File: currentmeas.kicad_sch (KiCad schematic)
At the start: 14 parts, among them U3 CSE7759B

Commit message: Renamed things. Removed reference image. Ready for the world.
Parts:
- U3: symbol merossspecific:CSE7759B -> designspecific:CSE7759B
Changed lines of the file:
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@@
 		)
 		(instances
-			(project "Meross smart outlet reverse"
+			(project "smart-outlet-m-reverse"
 				(path "/0b789f5a-74d1-4f81-bd1f-7ac838c6392e/64da09b2-a22e-4689-a149-b317ef83cf14"
 					(reference "R14")
@@
 		)
 		(instances
-			(project "Meross smart outlet reverse"
+			(project "smart-outlet-m-reverse"
 				(path "/0b789f5a-74d1-4f81-bd1f-7ac838c6392e/64da09b2-a22e-4689-a149-b317ef83cf14"
 					(reference "#PWR06")
@@
 		)
 		(instances
-			(project "Meross smart outlet reverse"
+			(project "smart-outlet-m-reverse"
 				(path "/0b789f5a-74d1-4f81-bd1f-7ac838c6392e/64da09b2-a22e-4689-a149-b317ef83cf14"
 					(reference "R13")
@@
 		)
 		(instances
-			(project "Meross smart outlet reverse"
+			(project "smart-outlet-m-reverse"
 				(path "/0b789f5a-74d1-4f81-bd1f-7ac838c6392e/64da09b2-a22e-4689-a149-b317ef83cf14"
 					(reference "C16")
@@
 		)
 		(instances
-			(project "Meross smart outlet reverse"
+			(project "smart-outlet-m-reverse"
 				(path "/0b789f5a-74d1-4f81-bd1f-7ac838c6392e/64da09b2-a22e-4689-a149-b317ef83cf14"
 					(reference "R15")
@@
 		)
 		(instances
-			(project "Meross smart outlet reverse"
+			(project "smart-outlet-m-reverse"
 				(path "/0b789f5a-74d1-4f81-bd1f-7ac838c6392e/64da09b2-a22e-4689-a149-b317ef83cf14"
 					(reference "R20")
@@
 		)
 		(instances
-			(project "Meross smart outlet reverse"
+			(project "smart-outlet-m-reverse"
 				(path "/0b789f5a-74d1-4f81-bd1f-7ac838c6392e/64da09b2-a22e-4689-a149-b317ef83cf14"
 					(reference "#PWR05")
@@
 		)
 		(instances
-			(project "Meross smart outlet reverse"
+			(project "smart-outlet-m-reverse"
 				(path "/0b789f5a-74d1-4f81-bd1f-7ac838c6392e/64da09b2-a22e-4689-a149-b317ef83cf14"
 					(reference "R16")
@@
 		)
 		(instances
-			(project "Meross smart outlet reverse"
+			(project "smart-outlet-m-reverse"
 				(path "/0b789f5a-74d1-4f81-bd1f-7ac838c6392e/64da09b2-a22e-4689-a149-b317ef83cf14"
 					(reference "#PWR04")
@@
 		)
 		(instances
-			(project "Meross smart outlet reverse"
+			(project "smart-outlet-m-reverse"
 				(path "/0b789f5a-74d1-4f81-bd1f-7ac838c6392e/64da09b2-a22e-4689-a149-b317ef83cf14"
 					(reference "#PWR019")
@@
 		)
 		(instances
-			(project "Meross smart outlet reverse"
+			(project "smart-outlet-m-reverse"
 				(path "/0b789f5a-74d1-4f81-bd1f-7ac838c6392e/64da09b2-a22e-4689-a149-b317ef83cf14"
 					(reference "C19")
@@
 	)
 	(symbol
-		(lib_id "merossspecific:CSE7759B")
+		(lib_id "designspecific:CSE7759B")
 		(at 170.18 85.09 0)
 		(unit 1)
@@
 		)
 		(instances
-			(project "Meross smart outlet reverse"
+			(project "smart-outlet-m-reverse"
 				(path "/0b789f5a-74d1-4f81-bd1f-7ac838c6392e/64da09b2-a22e-4689-a149-b317ef83cf14"
 					(reference "C18")
@@
 		)
 		(instances
-			(project "Meross smart outlet reverse"
+			(project "smart-outlet-m-reverse"
 				(path "/0b789f5a-74d1-4f81-bd1f-7ac838c6392e/64da09b2-a22e-4689-a149-b317ef83cf14"
 					(reference "R17")
@@
 		)
 		(instances
-			(project "Meross smart outlet reverse"
+			(project "smart-outlet-m-reverse"
 				(path "/0b789f5a-74d1-4f81-bd1f-7ac838c6392e/64da09b2-a22e-4689-a149-b317ef83cf14"
 					(reference "R12")
@@
 		)
 		(instances
-			(project "Meross smart outlet reverse"
+			(project "smart-outlet-m-reverse"
 				(path "/0b789f5a-74d1-4f81-bd1f-7ac838c6392e/64da09b2-a22e-4689-a149-b317ef83cf14"
 					(reference "R18")

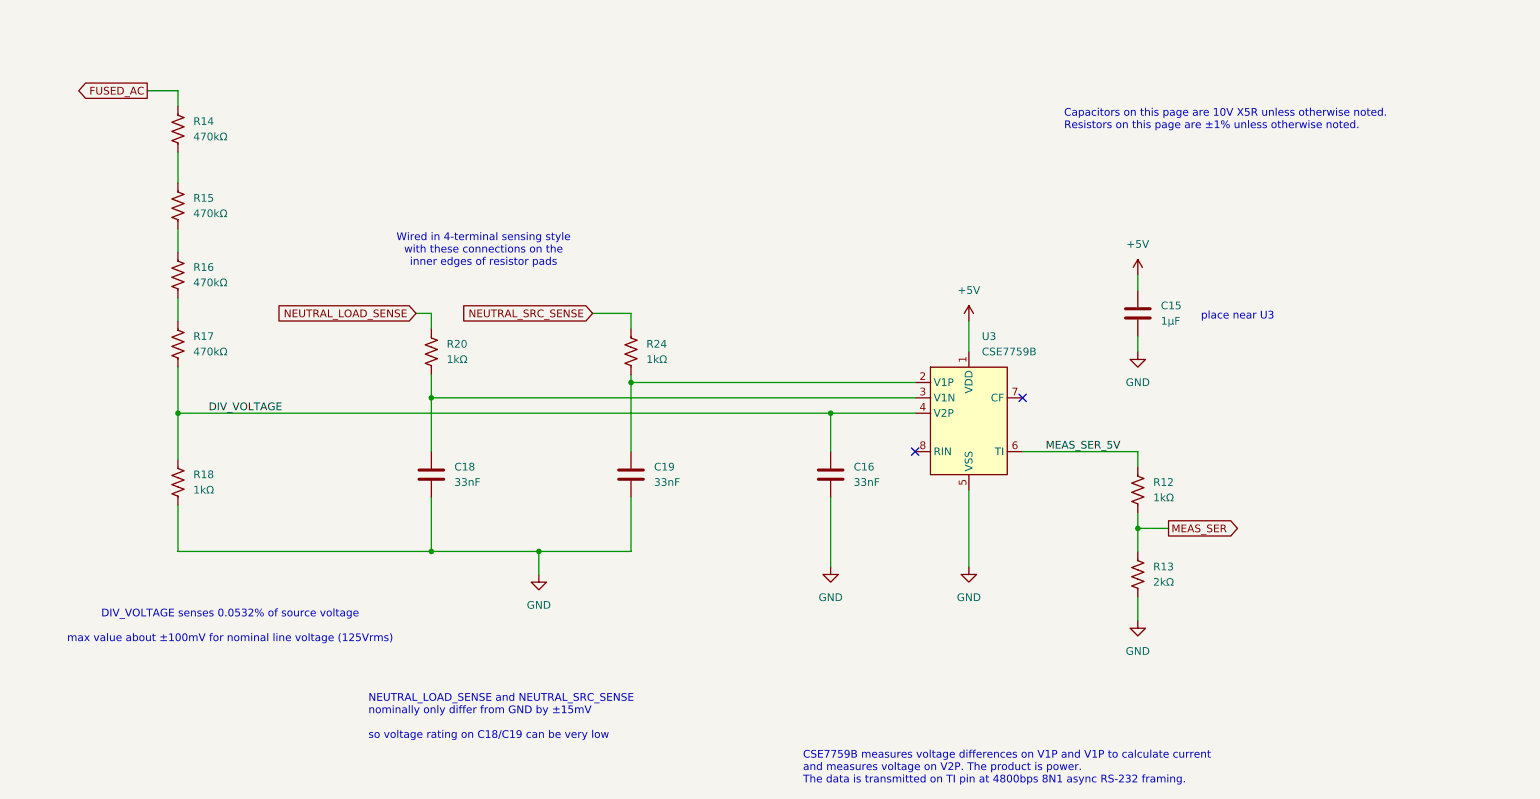
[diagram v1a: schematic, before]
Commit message: Rearranged SMPS circuit. Added a lot of schematic comments. Moved RECT_AC line away from NEUTRAL_SRC (not enough). Updated README greatly. Added pictures. Added PDF schematic.
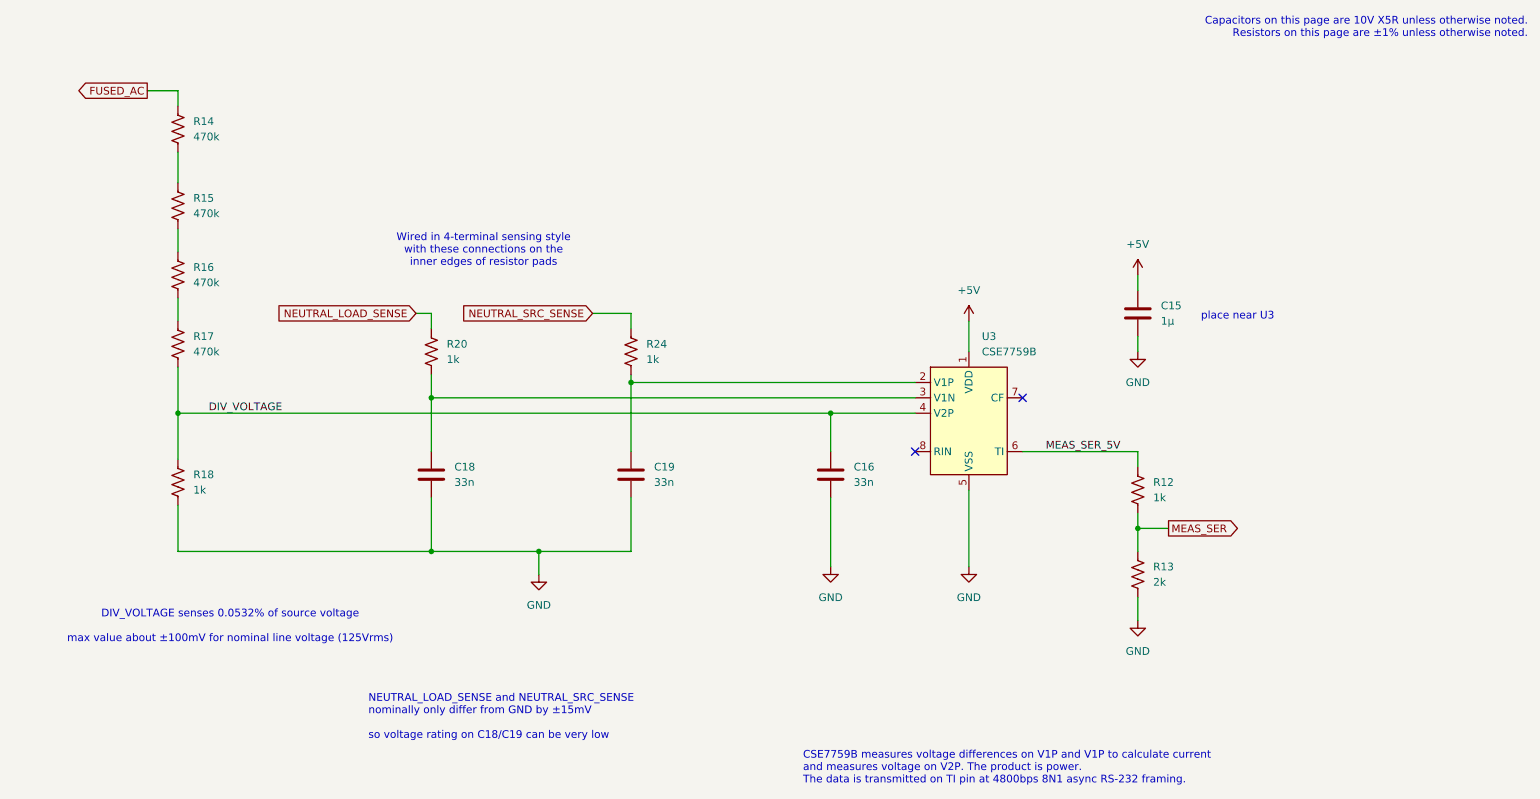
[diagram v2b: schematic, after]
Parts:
- C15: value 1µF -> 1µ
- C16, C18, C19: value 33nF -> 33n
- R12, R18, R20, R24: value 1kΩ -> 1k
- R13: value 2kΩ -> 2k
- R14, R15, R16, R17: value 470kΩ -> 470k
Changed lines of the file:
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@@
 	(paper "USLetter")
 	(title_block
-		(date "2025-07-28")
+		(date "2025-08-17")
+		(rev "a")
 	)
 	(text "NEUTRAL_LOAD_SENSE and NEUTRAL_SRC_SENSE\nnominally only differ from GND by ±15mV\n\nso voltage rating on C18/C19 can be very low"
@@
 	(text "Capacitors on this page are 10V X5R unless otherwise noted.\nResistors on this page are ±1% unless otherwise noted."
 		(exclude_from_sim no)
-		(at 185.928 35.306 0)
+		(at 262.636 20.066 0)
 		(effects
 			(font
 				(size 1.27 1.27)
 			)
-			(justify left)
+			(justify right)
 		)
 	)
@@
 			)
 		)
-		(property "Value" "470kΩ"
+		(property "Value" "470k"
 			(at 41.91 38.0999 0)
 			(effects
@@
 			)
 		)
-		(property "Value" "2kΩ"
+		(property "Value" "2k"
 			(at 200.66 111.7599 0)
 			(effects
@@
 			)
 		)
-		(property "Value" "33nF"
+		(property "Value" "33n"
 			(at 151.13 95.2499 0)
 			(effects
@@
 			)
 		)
-		(property "Value" "1µF"
+		(property "Value" "1µ"
 			(at 201.93 68.5799 0)
 			(effects
@@
 			)
 		)
-		(property "Value" "470kΩ"
+		(property "Value" "470k"
 			(at 41.91 50.7999 0)
 			(effects
@@
 			)
 		)
-		(property "Value" "1kΩ"
+		(property "Value" "1k"
 			(at 83.82 74.9299 0)
 			(effects
@@
 			)
 		)
-		(property "Value" "470kΩ"
+		(property "Value" "470k"
 			(at 41.91 62.2299 0)
 			(effects
@@
 			)
 		)
-		(property "Value" "33nF"
+		(property "Value" "33n"
 			(at 118.11 95.2499 0)
 			(effects
@@
 			)
 		)
-		(property "Value" "1kΩ"
+		(property "Value" "1k"
 			(at 116.84 74.9299 0)
 			(effects
@@
 			)
 		)
-		(property "Value" "33nF"
+		(property "Value" "33n"
 			(at 85.09 95.2499 0)
 			(effects
@@
 			)
 		)
-		(property "Value" "470kΩ"
+		(property "Value" "470k"
 			(at 41.91 73.6599 0)
 			(effects
@@
 			)
 		)
-		(property "Value" "1kΩ"
+		(property "Value" "1k"
 			(at 200.66 97.7899 0)
 			(effects
@@
 			)
 		)
-		(property "Value" "1kΩ"
+		(property "Value" "1k"
 			(at 41.91 96.5199 0)
 			(effects
